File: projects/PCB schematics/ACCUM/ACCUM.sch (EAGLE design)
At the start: 14 parts, among them IC2 78L08SMD, Q2 IRLZ44Z

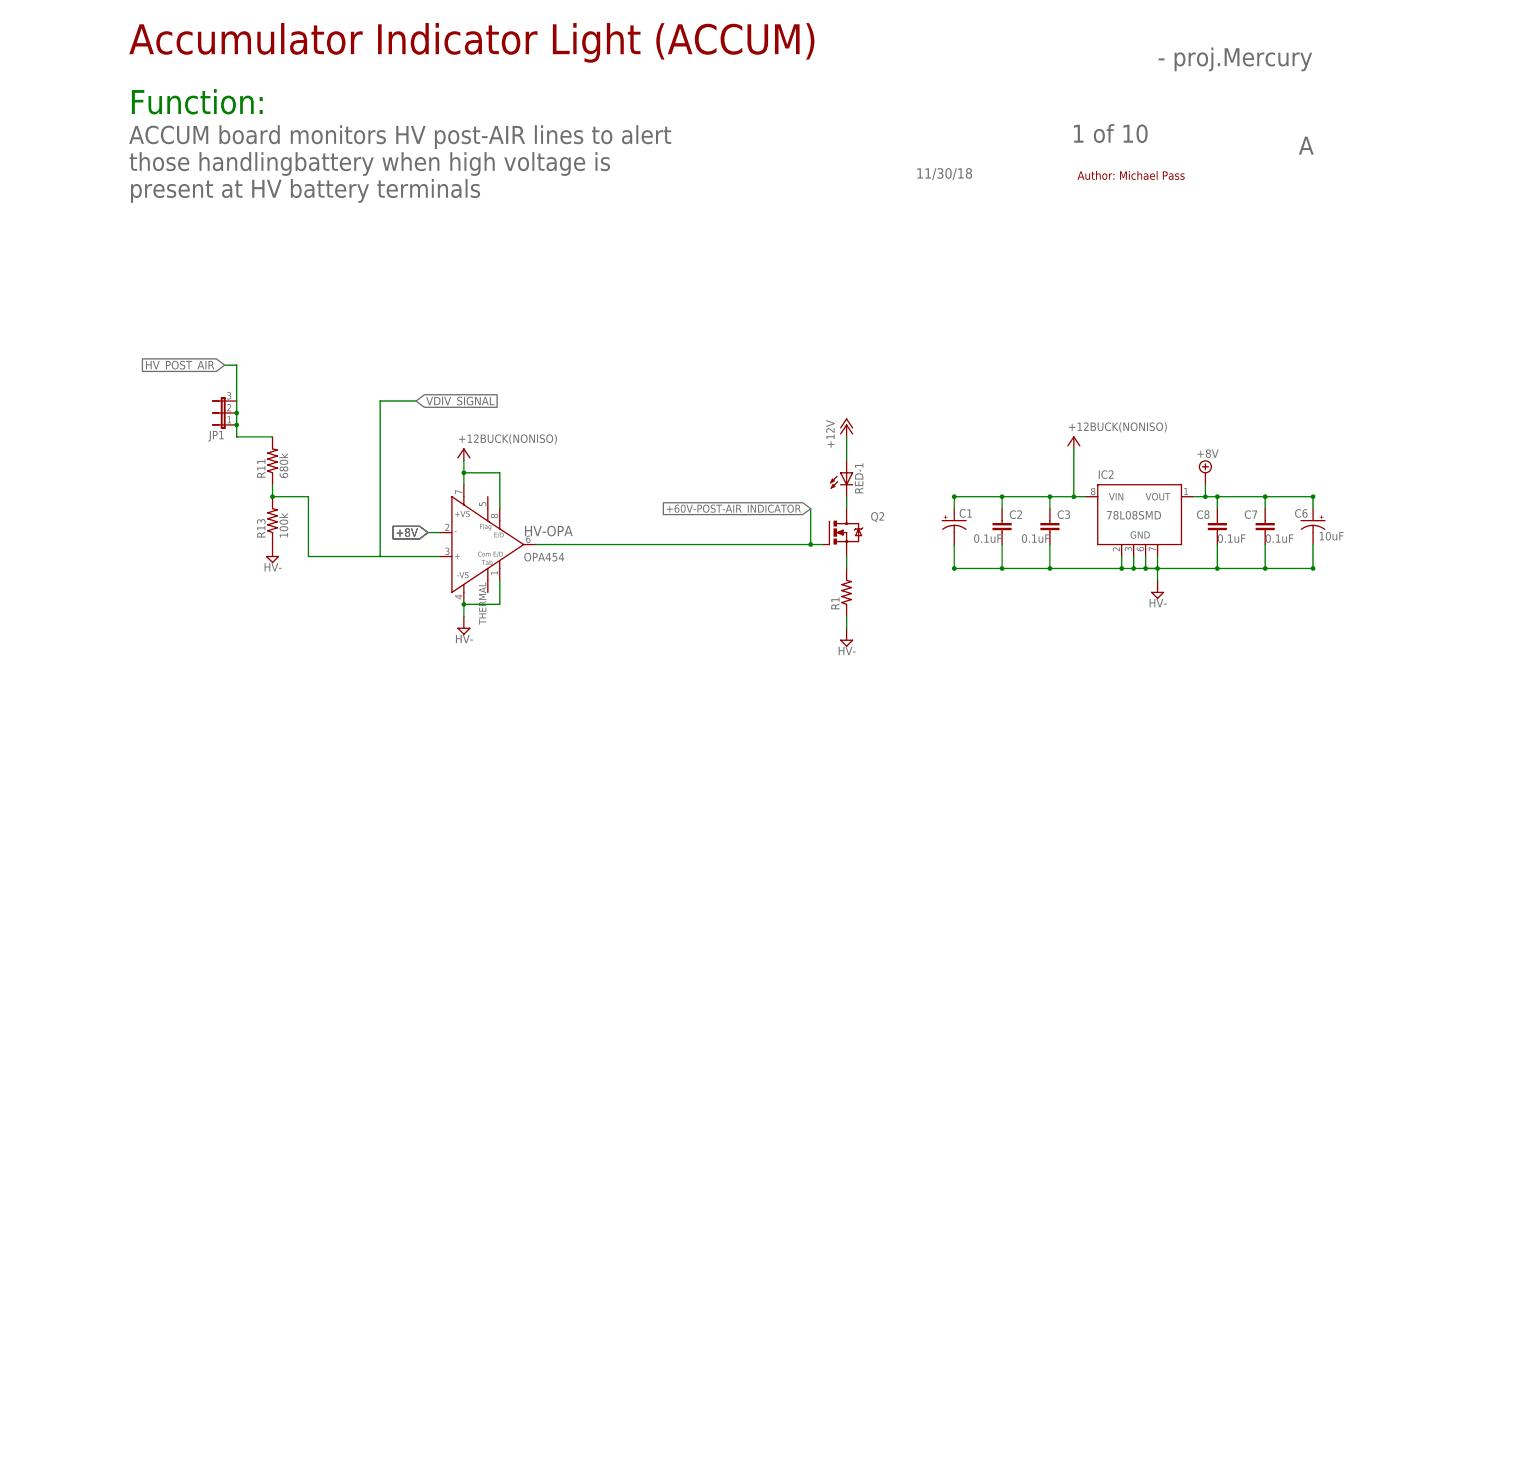
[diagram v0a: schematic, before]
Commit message: ACCUM - Initial schematic revision.
Schematics have still not been properly updated from ESF versions.
In this commit, I've added in some external connectors (LED, etc.)

---SQUASH---

ACCUM - Initial revision; break to checkout TSALC.
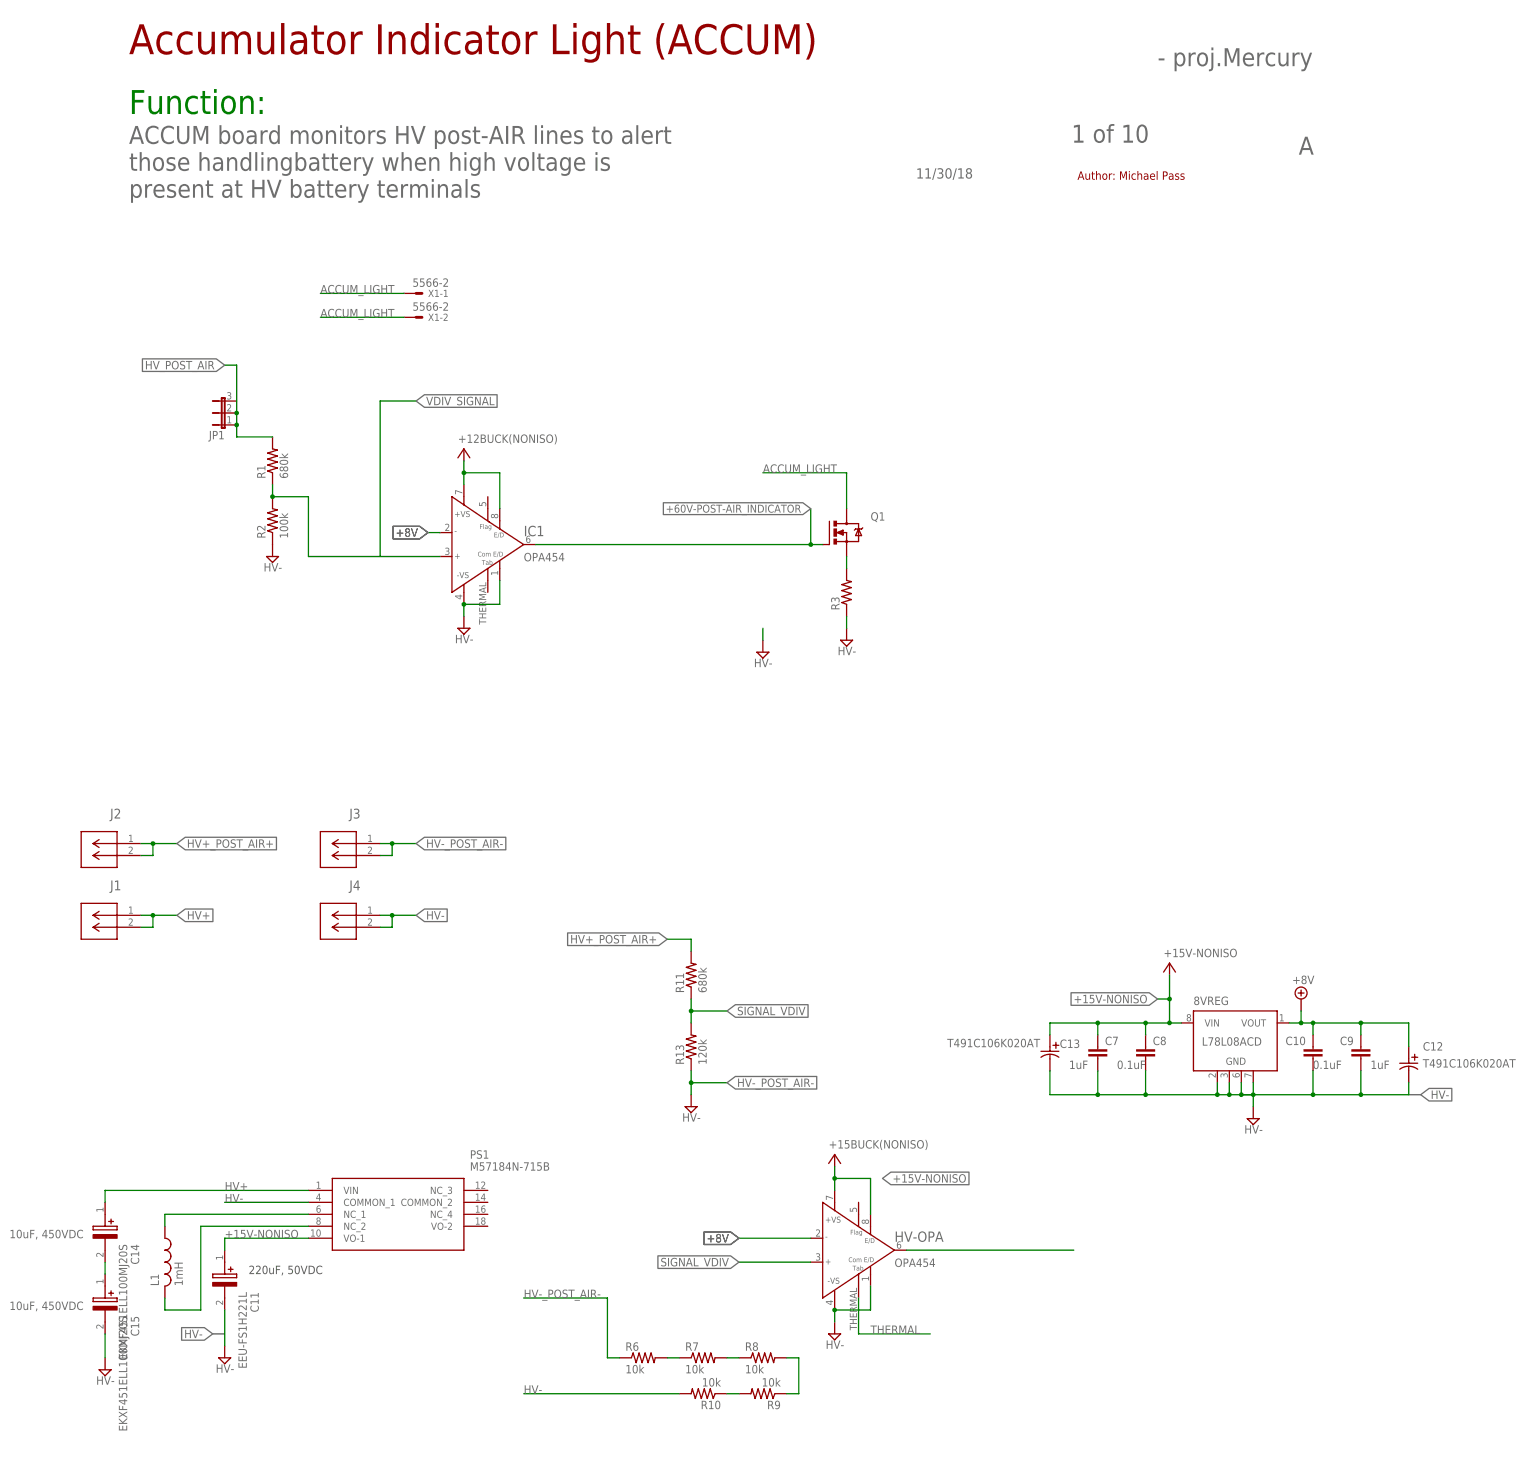
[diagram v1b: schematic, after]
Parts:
- removed C1, C6: 10uF, rcl:CPOL-US085CS-1AW
- removed C2, C3: 0.1uF, rcl:C-EUC0805
- removed IC2: 78L08SMD, linear:78L08SMD
- removed RED: LZR184, led:LZR184
- added 8VREG: L78L08ACD, linear:78L08SMD
- added C10: 0.1uF, rcl:C-EUC0805
- added C11: EEU-FS1H221L, EEU-FS1H221L:EEU-FS1H221L
- added C12, C13: T491C106K020AT, T491C106K020AT:T491C106K020AT
- added C14, C15: EKXF451ELL100MJ20S, EKXF451ELL100MJ20S:EKXF451ELL100MJ20S
- added C9: 1uF, rcl:C-EUC0805
- added IC1: OPA454, OPA454:OPA454
- added J1, J2, J3, J4: 2P_1-770166-0, con-MATE-N-LOK:2P_1-770166-0
- added L1: 1mH, rcl:L-USL2012C
- added PS1: M57184N-715B, M57184N-715B:M57184N-715B
- added R10, R6, R7, R8, R9: 10k, rcl:R-US_R0805
- added R2: 100k, rcl:R-US_R0805
- added R3: (no value), rcl:R-US_R0805
- added X1: 5566-2, con-molex:5566-2
- C7: value 0.1uF -> 1uF
- R1: value (none) -> 680k
- R13: value 100k -> 120k
- renumbered Q2 to Q1
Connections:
- removed net +12V: RED-1.A
- new net +15V-NONISO: 8VREGG$1.VIN, C11.+, C13.1, C7.1, C8.1, HV-OPA.+VS, HV-OPA.E/D, PS1.VO-1
- new net ACCUM_LIGHT: Q1.D, X1-1.S, X1-2.S
- new net HV+: C14.+, J1.1, J1.2, PS1.VIN
- new net HV+_POST_AIR+: J2.1, J2.2, R11.2
- new net HV-_POST_AIR-: J3.1, J3.2, R13.1, R6.1
- new net N$1: L1.2, PS1.NC_2
- new net N$3: C14.-, C15.+
- new net N$4: R7.2, R8.1
- new net N$5: R6.2, R7.1
- new net N$7: R8.2, R9.1
- new net N$8: R10.1, R9.2
- new net N$9: HV-OPA.OUT
- new net SIGNAL_VDIV: HV-OPA.IN+, R11.1, R13.2
- new net THERMAL: HV-OPA.E/DCOM1
- net +60V-POST-AIR_INDICATOR: now also IC1.OUT; no longer HV-OPA.OUT
- net +8V: now also 8VREGG$1.VOUT, C10.1, C12.1, C9.1, IC1.IN-; no longer C6.+, C7.1, C8.1, IC2G$1.VOUT
- net GND: now also R2.1, R3.1; no longer R1.1, R13.1
- net HV-: now also 8VREGG$1.GND@1, 8VREGG$1.GND@2, 8VREGG$1.GND@3, 8VREGG$1.GND@4, C10.2, C11.-, C12.2, C13.2, C15.-, C9.2, IC1.-VS, IC1.E/DCOM, J4.1, J4.2, PS1.COMMON_1, R10.2; no longer C1.-, C2.2, C3.2, C6.-, IC2G$1.GND@1, IC2G$1.GND@2, IC2G$1.GND@3, IC2G$1.GND@4
- net HV_POST_AIR: now also R1.2; no longer R11.2
- net N$2: now also L1.1, PS1.NC_1; no longer Q1.D, RED-1.C
- net N$6: now also R3.2; no longer R1.2
- net V+: now also IC1.+VS, IC1.E/D; no longer C1.+, C2.1, C3.1, HV-OPA.+VS, HV-OPA.E/D, IC2G$1.VIN
- net VDIV_SIGNAL: now also IC1.IN+, R1.1, R2.2; no longer HV-OPA.IN+, R11.1, R13.2
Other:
- note added: "10uF, 450VDC"
- note added: "220uF, 50VDC"
- moved on the sheet: C7, C8, HV-OPA, R1, R11, R13
